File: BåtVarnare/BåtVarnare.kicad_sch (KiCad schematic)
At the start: 10 parts, among them U1 SIM800C, U2 Buck converter, U3 Buck converter

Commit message: Uppdaterade sch
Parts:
- renumbered R1 to R1Nödvändig??
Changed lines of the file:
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@@
-	(wire
-		(pts
-			(xy 172.72 95.25) (xy 171.45 95.25)
-		)
-		(stroke
-			(width 0)
-			(type default)
-		)
-	)
 	(wire
 		(pts
@@
 		(on_board yes)
 		(dnp no)
-		(property "Reference" "R1"
+		(property "Reference" "R1Nödvändig??"
 			(at 173.736 95.25 90)
 			(effects
@@
 			(project ""
 				(path "/be6829d7-daf3-4649-8621-8128d8bc6168"
-					(reference "R1")
+					(reference "R1Nödvändig??")
 					(unit 1)
 				)

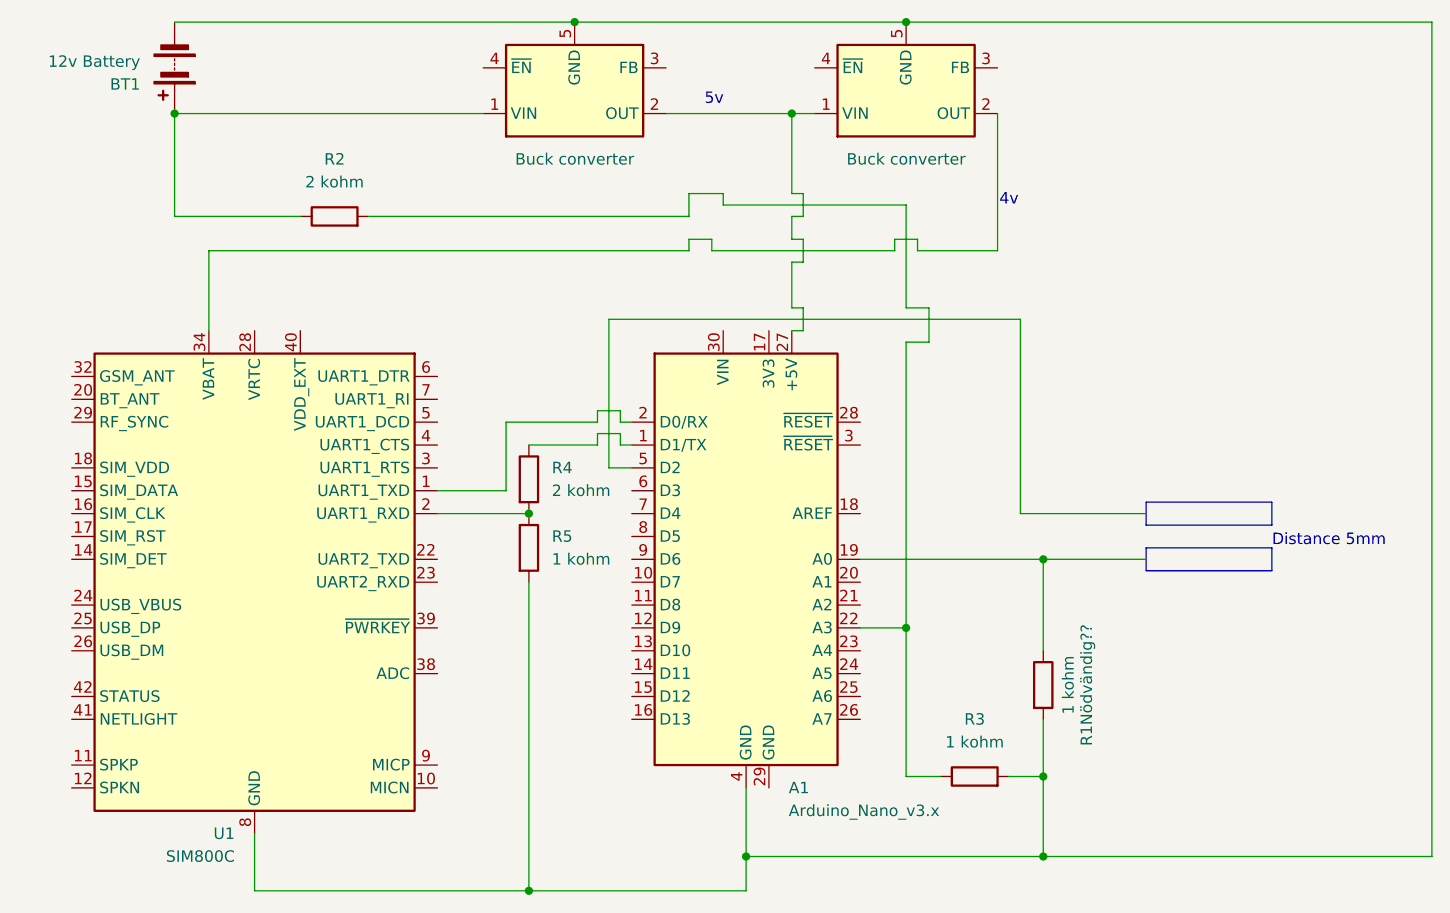
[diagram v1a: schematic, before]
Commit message: Updaterade schematic
Snyggade upp
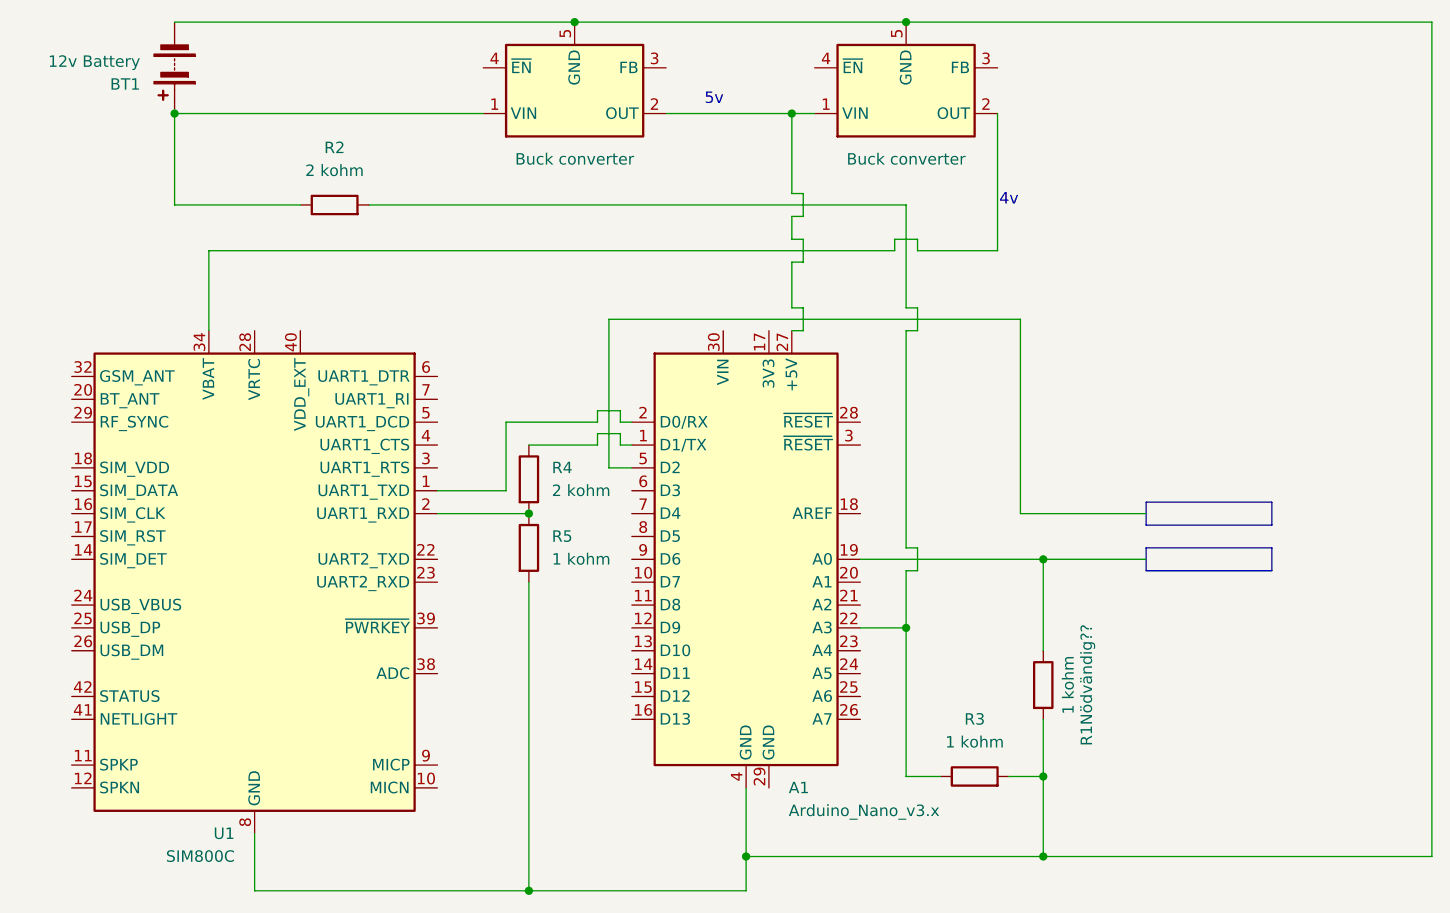
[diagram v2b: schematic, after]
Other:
- note removed: "Distance 5mm"
- company: (none) -> SIMACompany
- title: (none) -> SIMA
- moved on the sheet: R2
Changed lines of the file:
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@@
 	(generator_version "8.0")
 	(paper "A4")
+	(title_block
+		(title "SIMA")
+		(date "2025-01-02")
+		(rev "1")
+		(company "SIMACompany")
+	)
 	(junction
 		(at 111.76 118.11)
@@
 	(wire
 		(pts
-			(xy 129.54 40.64) (xy 133.35 40.64)
-		)
-		(stroke
-			(width 0)
-			(type default)
-		)
-	)
-	(wire
-		(pts
 			(xy 81.28 118.11) (xy 111.76 118.11)
 		)
@@
 	(wire
 		(pts
-			(xy 156.21 53.34) (xy 156.21 57.15)
-		)
-		(stroke
-			(width 0)
-			(type default)
-		)
-	)
-	(wire
-		(pts
-			(xy 72.39 31.75) (xy 72.39 43.18)
+			(xy 154.94 53.34) (xy 154.94 55.88)
+		)
+		(stroke
+			(width 0)
+			(type default)
+		)
+	)
+	(wire
+		(pts
+			(xy 72.39 31.75) (xy 72.39 41.91)
 		)
 		(stroke
@@
 	(wire
 		(pts
+			(xy 154.94 82.55) (xy 153.67 82.55)
+		)
+		(stroke
+			(width 0)
+			(type default)
+		)
+	)
+	(wire
+		(pts
 			(xy 154.94 45.72) (xy 152.4 45.72)
 		)
@@
 	(wire
 		(pts
-			(xy 129.54 43.18) (xy 129.54 40.64)
-		)
-		(stroke
-			(width 0)
-			(type default)
-		)
-	)
-	(wire
-		(pts
 			(xy 140.97 31.75) (xy 140.97 40.64)
 		)
@@
 	(wire
 		(pts
-			(xy 152.4 46.99) (xy 132.08 46.99)
-		)
-		(stroke
-			(width 0)
-			(type default)
-		)
-	)
-	(wire
-		(pts
 			(xy 140.97 53.34) (xy 140.97 48.26)
 		)
@@
 	(wire
 		(pts
+			(xy 153.67 80.01) (xy 154.94 80.01)
+		)
+		(stroke
+			(width 0)
+			(type default)
+		)
+	)
+	(wire
+		(pts
 			(xy 121.92 67.31) (xy 121.92 68.58)
 		)
@@
 	(wire
 		(pts
-			(xy 132.08 45.72) (xy 129.54 45.72)
-		)
-		(stroke
-			(width 0)
-			(type default)
-		)
-	)
-	(wire
-		(pts
 			(xy 168.91 81.28) (xy 180.34 81.28)
 		)
@@
 	(wire
 		(pts
-			(xy 153.67 57.15) (xy 153.67 88.9)
-		)
-		(stroke
-			(width 0)
-			(type default)
-		)
-	)
-	(wire
-		(pts
-			(xy 129.54 45.72) (xy 129.54 46.99)
-		)
-		(stroke
-			(width 0)
-			(type default)
-		)
-	)
-	(wire
-		(pts
 			(xy 109.22 66.04) (xy 119.38 66.04)
 		)
@@
 	(wire
 		(pts
-			(xy 153.67 53.34) (xy 156.21 53.34)
+			(xy 153.67 53.34) (xy 154.94 53.34)
 		)
 		(stroke
@@
 	(wire
 		(pts
-			(xy 93.98 43.18) (xy 129.54 43.18)
-		)
-		(stroke
-			(width 0)
-			(type default)
-		)
-	)
-	(wire
-		(pts
-			(xy 132.08 46.99) (xy 132.08 45.72)
-		)
-		(stroke
-			(width 0)
-			(type default)
-		)
-	)
-	(wire
-		(pts
-			(xy 156.21 57.15) (xy 153.67 57.15)
+			(xy 93.98 41.91) (xy 153.67 41.91)
+		)
+		(stroke
+			(width 0)
+			(type default)
+		)
+	)
+	(wire
+		(pts
+			(xy 154.94 55.88) (xy 153.67 55.88)
 		)
 		(stroke
@@
 	(wire
 		(pts
+			(xy 153.67 82.55) (xy 153.67 88.9)
+		)
+		(stroke
+			(width 0)
+			(type default)
+		)
+	)
+	(wire
+		(pts
 			(xy 168.91 114.3) (xy 135.89 114.3)
 		)
@@
 	(wire
 		(pts
-			(xy 129.54 46.99) (xy 76.2 46.99)
+			(xy 76.2 46.99) (xy 152.4 46.99)
 		)
 		(stroke
@@
 	(wire
 		(pts
-			(xy 133.35 41.91) (xy 153.67 41.91)
+			(xy 153.67 55.88) (xy 153.67 80.01)
+		)
+		(stroke
+			(width 0)
+			(type default)
+		)
+	)
+	(wire
+		(pts
+			(xy 154.94 80.01) (xy 154.94 82.55)
 		)
 		(stroke
@@
 	(wire
 		(pts
-			(xy 133.35 40.64) (xy 133.35 41.91)
-		)
-		(stroke
-			(width 0)
-			(type default)
-		)
-	)
-	(wire
-		(pts
 			(xy 111.76 118.11) (xy 135.89 118.11)
 		)
@@
 	(wire
 		(pts
-			(xy 72.39 43.18) (xy 86.36 43.18)
+			(xy 72.39 41.91) (xy 86.36 41.91)
 		)
 		(stroke
@@
 		(exclude_from_sim no)
 		(at 165.1 41.402 0)
-		(effects
-			(font
-				(size 1.27 1.27)
-			)
-		)
-	)
-	(text "Distance 5mm"
-		(exclude_from_sim no)
-		(at 200.66 79.248 0)
 		(effects
 			(font
@@
 	(symbol
 		(lib_id "Device:R")
-		(at 90.17 43.18 90)
+		(at 90.17 41.91 90)
 		(unit 1)
 		(exclude_from_sim no)
@@
 		(fields_autoplaced yes)
 		(property "Reference" "R2"
-			(at 90.17 36.83 90)
+			(at 90.17 35.56 90)
 			(effects
 				(font
@@
 		)
 		(property "Value" "2 kohm"
-			(at 90.17 39.37 90)
+			(at 90.17 38.1 90)
 			(effects
 				(font
@@
 		)
 		(property "Footprint" ""
-			(at 90.17 44.958 90)
+			(at 90.17 43.688 90)
 			(effects
 				(font
@@
 		)
 		(property "Datasheet" "~"
-			(at 90.17 43.18 0)
+			(at 90.17 41.91 0)
 			(effects
 				(font
@@
 		)
 		(property "Description" "Resistor"
-			(at 90.17 43.18 0)
-			(effects
-				(font
+			(at 90.17 41.91 0)
+			(effects
+				(font

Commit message: Lade till LED
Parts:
- added D1: LED, symbol Device:LED
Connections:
- net at A1.4 (GND), BT1.2 (-), R1Nödvändig??.2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: now also D1.1 (K)
- net at A1.16 (D13): now also D1.2 (A)
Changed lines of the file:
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@@
+	)
+	(junction
+		(at 119.38 118.11)
+		(diameter 0)
+		(color 0 0 0 0)
 	)
 	(junction
@@
 	(wire
 		(pts
+			(xy 119.38 99.06) (xy 119.38 105.41)
+		)
+		(stroke
+			(width 0)
+			(type default)
+		)
+	)
+	(wire
+		(pts
 			(xy 142.24 45.72) (xy 140.97 45.72)
 		)
@@
 	(wire
 		(pts
+			(xy 119.38 118.11) (xy 135.89 118.11)
+		)
+		(stroke
+			(width 0)
+			(type default)
+		)
+	)
+	(wire
+		(pts
 			(xy 109.22 73.66) (xy 109.22 66.04)
 		)
@@
 	(wire
 		(pts
+			(xy 119.38 113.03) (xy 119.38 118.11)
+		)
+		(stroke
+			(width 0)
+			(type default)
+		)
+	)
+	(wire
+		(pts
 			(xy 140.97 53.34) (xy 140.97 48.26)
 		)
@@
 	(wire
 		(pts
+			(xy 123.19 99.06) (xy 119.38 99.06)
+		)
+		(stroke
+			(width 0)
+			(type default)
+		)
+	)
+	(wire
+		(pts
 			(xy 153.67 55.88) (xy 153.67 80.01)
 		)
@@
 	(wire
 		(pts
-			(xy 111.76 118.11) (xy 135.89 118.11)
+			(xy 111.76 118.11) (xy 119.38 118.11)
 		)
 		(stroke
@@
 					(unit 1)
 				)
+			)
+		)
+	)
+	(symbol
+		(lib_id "Device:LED")
+		(at 119.38 109.22 90)
+		(unit 1)
+		(exclude_from_sim no)
+		(in_bom yes)
+		(on_board yes)
+		(dnp no)
+		(fields_autoplaced yes)
+		(property "Reference" "D1"
+			(at 123.19 109.5374 90)
+			(effects
+				(font
+					(size 1.27 1.27)
+				)
+				(justify right)
+			)
+		)
+		(property "Value" "LED"
+			(at 123.19 112.0774 90)
+			(effects
+				(font
+					(size 1.27 1.27)
+				)
+				(justify right)
+			)
+		)
+		(property "Footprint" ""
+			(at 119.38 109.22 0)
+			(effects
+				(font
+					(size 1.27 1.27)
+				)
+				(hide yes)
+			)
+		)
+		(property "Datasheet" "~"
+			(at 119.38 109.22 0)
+			(effects
+				(font
+					(size 1.27 1.27)
+				)
+				(hide yes)
+			)
+		)
+		(property "Description" "Light emitting diode"
+			(at 119.38 109.22 0)
+			(effects
+				(font
+					(size 1.27 1.27)
+				)
+				(hide yes)
+			)
+		)
+		(pin "1"
+		)
+		(pin "2"
+		)
+		(instances
+			(project ""
+				(path "/be6829d7-daf3-4649-8621-8128d8bc6168"
+					(reference "D1")
+					(unit 1)
+				)
